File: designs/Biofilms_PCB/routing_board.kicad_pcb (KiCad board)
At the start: 2 copper layers, 53.3 x 66 mm, 12 parts, among them J1 Conn_01x08, J10 Conn_01x12, J11 Barrel_Jack, J2 Conn_01x06, J3 Conn_01x02, J4 Conn_01x10, J5 Conn_01x08, J6 Conn_01x03, J7 Conn_01x04, J8 Conn_01x10, J9 Conn_01x02, K1 RLY_5VCoil_PB1064CT

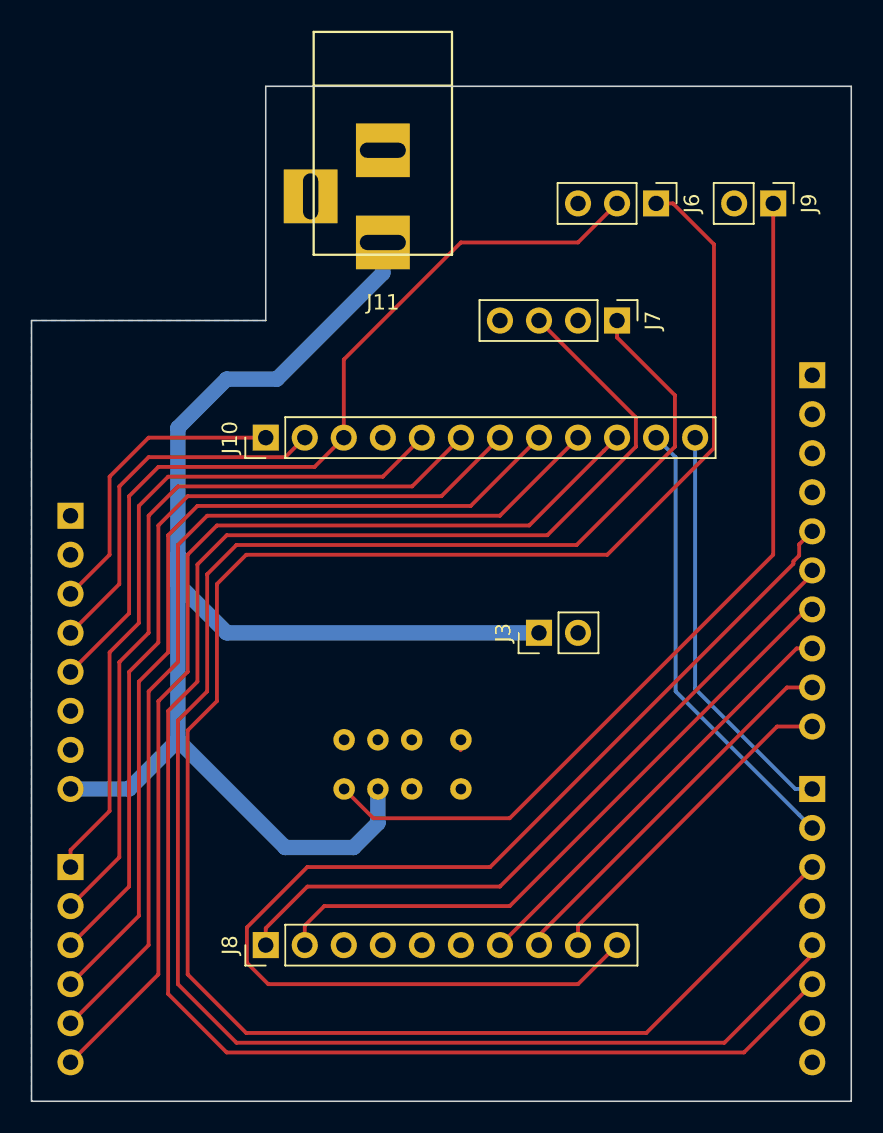
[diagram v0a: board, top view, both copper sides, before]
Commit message: finalized v1 of biofilms PCB
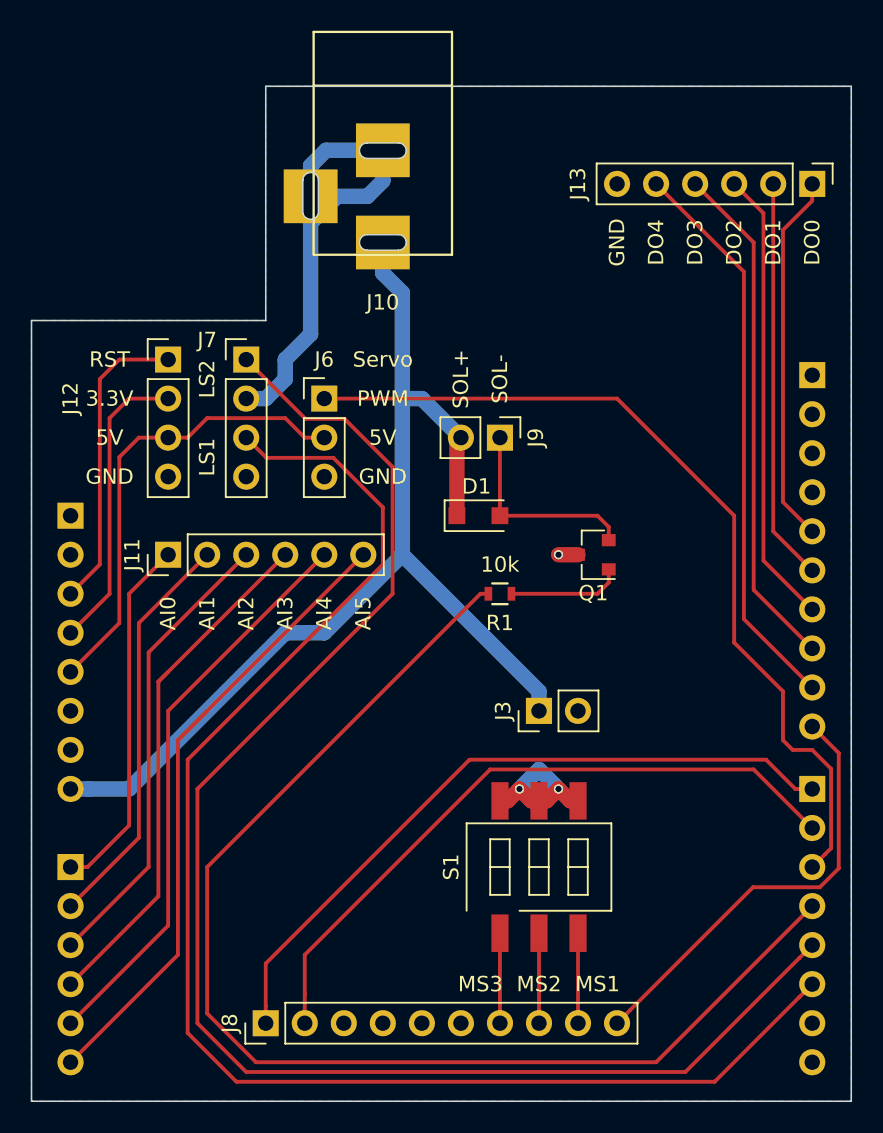
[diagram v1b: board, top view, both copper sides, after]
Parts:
- removed K1: RLY_5VCoil_PB1064CT, Relays_THT:Relay_DPDT_AXICOM_IMSeries_Pitch3.2mm
- added D1: D, Diodes_SMD:D_SOD-123F, F.Cu at (54.5, 78.7)
- added J12: Arduino Power Out, Pin_Headers:Pin_Header_Straight_1x04_Pitch2.54mm, F.Cu at (34.3, 68.6)
- added J13: Digital Out, Pin_Headers:Pin_Header_Straight_1x06_Pitch2.54mm, F.Cu at (76.2, 57.1)
- added Q1: Q_NPN_Darlington_BCE, TO_SOT_Packages_SMD:SOT-23, F.Cu at (62.0, 81.3)
- added R1: 10k, Resistors_SMD:R_0603, F.Cu at (55.9, 83.8)
- added S1: Dip_Switch_3, Buttons_Switches_SMD:SW_DIP_x3_W8.61mm_Slide_LowProfile, F.Cu at (58.4, 101.6)
- J1: value Conn_01x08 -> Arduino TL
- J10: value Conn_01x12 -> DC PWR; footprint Socket_Strips:Socket_Strip_Straight_1x12_Pitch2.54mm -> Connectors:BARREL_JACK
- J11: value Barrel_Jack -> Analog In; footprint Connectors:BARREL_JACK -> Pin_Headers:Pin_Header_Straight_1x06_Pitch2.54mm
- J2: value Conn_01x06 -> Arduino BL
- J3: value Conn_01x02 -> Motor Power
- J4: value Conn_01x10 -> Arduino TR
- J5: value Conn_01x08 -> Arduino BR
- J6: value Conn_01x03 -> Servo
- J7: value Conn_01x04 -> Limit Switch
- J8: value Conn_01x10 -> Motor Driver
- J9: value Conn_01x02 -> Solenoid
- moved J11 30.0 mm to (34.3, 81.3), turned to 90 degrees
- moved J6 25.0 mm to (44.5, 71.1), turned to 0 degrees
- moved J7 24.3 mm to (39.4, 68.6), turned to 0 degrees
- moved J9 23.4 mm to (55.9, 73.7)
- moved J10 20.4 mm to (48.3, 54.8), turned to 270 degrees
- moved J3 5.08 mm to (58.4, 91.4)
- moved J8 5.08 mm to (40.6, 111.8)
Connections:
- J1 pad 1: Net-(J1-Pad1) -> (no net)
- J1 pad 2: Net-(J1-Pad2) -> (no net)
- J10 pad 1: /RESET -> +12V
- J10 pad 2: /3.3_OUT -> GND
- J10 pad 3: /5V_OUT -> GND
- J11 pad 1: +12V -> /AI0
- J11 pad 2: GND -> /AI1
- J11 pad 3: GND -> /AI2
- J4 pad 1: Net-(J4-Pad1) -> (no net)
- J4 pad 10: /MS1 -> /ENABLE
- J4 pad 2: Net-(J4-Pad2) -> (no net)
- J4 pad 3: Net-(J4-Pad3) -> (no net)
- J4 pad 4: Net-(J4-Pad4) -> (no net)
- J4 pad 5: /ENABLE -> /DO0
- J4 pad 6: /STEP -> /DO1
- J4 pad 7: /DIR -> /DO2
- J4 pad 8: /MS3 -> /DO3
- J4 pad 9: /MS2 -> /DO4
- J5 pad 1: /DO1 -> /STEP
- J5 pad 2: /DO0 -> /DIR
- J5 pad 4: /COIL+ -> /SOL_BASE
- J5 pad 7: Net-(J5-Pad7) -> (no net)
- J5 pad 8: Net-(J5-Pad8) -> (no net)
- J8 pad 4: Net-(J8-Pad4) -> (no net)
- J8 pad 5: Net-(J8-Pad5) -> (no net)
- J8 pad 6: Net-(J8-Pad6) -> (no net)
- J9 pad 1: /SOLENOID -> Net-(D1-Pad2)
- J9 pad 2: GND -> +12V
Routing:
- net /SOL_BASE: track 0.00 -> 80.1 mm
- net /SERVO_PWM: track 127.0 -> 56.5 mm
- net /SOLENOID: track 58.7 -> 0.00 mm
- net /ENABLE: track 76.0 -> 28.5 mm
- net GND: track 0.68 -> 41.8 mm, vias 0 -> 3
- net /DO4: track 0.00 -> 37.0 mm
- net /DO3: track 0.00 -> 33.4 mm
- net /DO2: track 0.00 -> 29.8 mm
- net /AI4: track 62.9 -> 37.3 mm
- net /5V_OUT: track 55.6 -> 30.2 mm
- net /AI2: track 54.3 -> 30.1 mm
- net /AI3: track 58.6 -> 34.6 mm
- net /AI5: track 67.3 -> 43.6 mm
- net /AI1: track 49.9 -> 26.5 mm
- net /MS3: track 28.3 -> 5.86 mm
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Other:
- outline, holes or cut-outs redrawn
- board text added: "3.3V"
- board text added: "5V"
- board text added: "AI0"
- board text added: "AI1"
- board text added: "AI2"
- board text added: "AI3"
- board text added: "AI4"
- board text added: "AI5"
- board text added: "Biofilm Project: Motor Driver Adapter for Kathy Yang, UCSF Robert Puccinelli Chan-Zuckerberg Biohub 20180427 Rev A"
- board text added: "DO0"
- board text added: "DO1"
- board text added: "DO2"
- board text added: "DO3"
- board text added: "DO4"
- board text added: "GND"
- board text added: "LS1"
- board text added: "LS2"
- board text added: "MS1"
- board text added: "MS2"
- board text added: "MS3"
- board text added: "PWM"
- board text added: "RST"
- board text added: "SOL+"
- board text added: "SOL-"
- board text added: "Servo"

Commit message: finalized v2 of biofilms PCB
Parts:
- added D2: D, Diodes_SMD:D_SOD-123F, F.Cu at (54.5, 78.7)
- added D3: LED, LEDs:LED_0603_HandSoldering, F.Cu at (64.1, 76.7)
- added D4: LED, LEDs:LED_0603_HandSoldering, F.Cu at (71.8, 56.7)
- added D5: LED, LEDs:LED_0603_HandSoldering, F.Cu at (69.2, 56.7)
- added D6: LED, LEDs:LED_0603_HandSoldering, F.Cu at (66.7, 56.7)
- added D7: LED, LEDs:LED_0603_HandSoldering, F.Cu at (64.1, 56.7)
- added D8: LED, LEDs:LED_0603_HandSoldering, F.Cu at (61.6, 56.7)
- added D9: LED, LEDs:LED_0603_HandSoldering, F.Cu at (71.1, 97.0)
- added Q2: Q_PNP_BEC, TO_SOT_Packages_SMD:SOT-23, F.Cu at (60.3, 99.7)
- added R10: 2.5k, Resistors_SMD:R_0603_HandSoldering, F.Cu at (60.5, 95.2)
- added R2: 150k, Resistors_SMD:R_0603_HandSoldering, F.Cu at (55.9, 83.8)
- added R3: 2.5k, Resistors_SMD:R_0603_HandSoldering, F.Cu at (61.6, 74.5)
- added R4: 2.5k, Resistors_SMD:R_0603_HandSoldering, F.Cu at (71.8, 61.1)
- added R5: 2.5k, Resistors_SMD:R_0603_HandSoldering, F.Cu at (69.2, 61.1)
- added R6: 2.5k, Resistors_SMD:R_0603_HandSoldering, F.Cu at (66.7, 61.1)
- added R7: 2.5k, Resistors_SMD:R_0603_HandSoldering, F.Cu at (64.1, 61.1)
- added R8: 2.5k, Resistors_SMD:R_0603_HandSoldering, F.Cu at (61.6, 61.1)
- added R9: 150k, Resistors_SMD:R_0603_HandSoldering, F.Cu at (60.5, 104.1)
- D1: value D -> LED; footprint Diodes_SMD:D_SOD-123F -> LEDs:LED_0603_HandSoldering
- J10: value DC PWR -> Solenoid; footprint Connectors:BARREL_JACK -> Socket_Strips:Socket_Strip_Straight_1x02_Pitch2.54mm
- J12: value Arduino Power Out -> DC PWR; footprint Pin_Headers:Pin_Header_Straight_1x04_Pitch2.54mm -> Connectors:BARREL_JACK
- J7: value Limit Switch -> Motor Driver; footprint Socket_Strips:Socket_Strip_Straight_1x04_Pitch2.54mm -> Pin_Headers:Pin_Header_Straight_1x10_Pitch2.54mm
- J8: value Motor Driver -> Limit Switch; footprint Pin_Headers:Pin_Header_Straight_1x10_Pitch2.54mm -> Socket_Strips:Socket_Strip_Straight_1x04_Pitch2.54mm
- J9: value Solenoid -> Arduino Power Out; footprint Socket_Strips:Socket_Strip_Straight_1x02_Pitch2.54mm -> Pin_Headers:Pin_Header_Straight_1x04_Pitch2.54mm
- R1: value 10k -> 2.5k; footprint Resistors_SMD:R_0603 -> Resistors_SMD:R_0603_HandSoldering
- moved J7 49.5 mm to (63.5, 111.8), turned to 270 degrees
- moved J8 43.2 mm to (39.4, 68.6), turned to 0 degrees
- moved R1 25.4 mm to (56.7, 58.4)
- moved D1 23.0 mm to (56.7, 55.9)
- moved J9 22.2 mm to (34.3, 68.6), turned to 0 degrees
- moved J10 20.4 mm to (55.9, 73.7)
- moved J12 19.7 mm to (48.3, 54.8), turned to 270 degrees
- moved S1 10.2 mm to (48.3, 102.2)
- moved J13 9.38 mm to (71.8, 65.4)
- moved J3 2.54 mm to (61.0, 91.4), turned to 270 degrees
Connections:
- D1 pad 1: +12V -> GND
- J10 pad 1: +12V -> Net-(D2-Pad2)
- J10 pad 2: GND -> +12V
- J12 pad 1: /RESET -> +12V
- J12 pad 2: /3.3_OUT -> GND
- J12 pad 3: /5V_OUT -> GND
- J7 pad 1: /LS2_PULLUP -> /STEP
- J7 pad 2: GND -> /DIR
- J7 pad 3: /LS1_PULLUP -> GND
- J7 pad 4: GND -> /MC_5V
- J8 pad 1: /STEP -> /LS2_PULLUP
- J8 pad 2: /DIR -> GND
- J8 pad 3: GND -> /LS1_PULLUP
- J8 pad 4: (no net) -> GND
- J9 pad 1: Net-(D1-Pad2) -> /RESET
- J9 pad 2: +12V -> /3.3_OUT
- Q1 pad 2: Net-(D1-Pad2) -> Net-(D2-Pad2)
- R1 pad 1: Net-(Q1-Pad1) -> Net-(D1-Pad2)
- R1 pad 2: /SOL_BASE -> +12V
- S1 pad 1: /MS3 -> /MS1
- S1 pad 3: /MS1 -> /MS3
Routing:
- net /ENABLE: track 28.5 -> 77.3 mm
- net /STEP: track 45.7 -> 20.5 mm
- net +12V: track 72.6 -> 93.1 mm
- net /DIR: track 44.0 -> 23.6 mm
- net Net-(D2-Pad2): track 0.00 -> 15.8 mm
- net /MC_5V: track 0.00 -> 15.3 mm
- net Net-(D9-Pad2): track 0.00 -> 13.7 mm
- net Net-(D1-Pad2): track 13.3 -> 2.54 mm
- net Net-(D9-Pad1): track 0.00 -> 9.79 mm
- net GND: track 41.8 -> 50.8 mm, vias 3 -> 5
- net Net-(Q2-Pad1): track 0.00 -> 3.61 mm
- net /DO3: track 33.4 -> 30.1 mm
- net /DO4: track 37.0 -> 33.7 mm
- net /DO2: track 29.8 -> 26.6 mm
- net Net-(D3-Pad2): track 0.00 -> 2.54 mm
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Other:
- board text added: "Biofilm Project: Motor Driver Adapter for Kathy Yang, UCSF Robert Puccinelli Chan-Zuckerberg Biohub 20180430 Rev B"
- board text added: "DO10"
- board text added: "DO11"
- board text added: "DO12"
- board text added: "DO13"
- board text added: "DO6"
- board text added: "DO7"
- board text added: "DO8"
- board text added: "DO9"
- board text added: "ENABLE"
- board text added: "H"
- board text added: "L"
- board text added: "POWER"
- board text removed: "Biofilm Project: Motor Driver Adapter for Kathy Yang, UCSF Robert Puccinelli Chan-Zuckerberg Biohub 20180427 Rev A"
- board text removed: "DO0"
- board text removed: "DO1"
- board text removed: "DO2"
- board text removed: "DO3"
- board text removed: "DO4"
